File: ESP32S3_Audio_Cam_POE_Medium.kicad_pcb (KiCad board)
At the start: 2 copper layers, 97.8 x 70.5 mm, 241 parts, among them CN1 PJ-316C-6A, J1 Connector, USB-TYPE-C-16P, J10 Conn_01x02, J11 Conn_01x03, J12 Conn_01x02, J13 Conn_01x02, J14 Conn_01x03, J15 Conn_01x02, J16 Conn_01x02, J17 Conn_01x20_Pin, J18 Conn_01x20_Pin, J2 Conn_01x02, J3 Conn_01x02, J4 Conn_01x02, J5 Conn_01x02, J6 Conn_01x02, J7 Conn_01x03, J8 Conn_01x03, J9 Conn_01x02, Q1 AO3401A, Q2 AO3401A, Q3 AO3401A, Q4 AO3401A, Q5 AO3401A, Q6 AO3401A, Q7 AO3401A, U1 MT9221CT-06BR5, U10 ICS-43434, U11 ICS-43434, U3 USBLC6-2SC6, U4 ESP32-S3, U5 AXP2101, U6 DS18B20U(UMW), U7 W25Q128JVSIQ, U8 MAX98357AETE+T, U9 TM1637, Y1 40MHz, 15pF, Y2 32.768KHz

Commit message: DRAFT Medium
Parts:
- removed R12, R15: 100kΩ, PCM_JLCPCB:R_0402
- removed R14, R16: 10kΩ, PCM_JLCPCB:R_0402
- removed TP26: TestPoint, TestPoint:TestPoint_Pad_D1.0mm
- added J19: Conn_01x03, Connector_PinHeader_2.54mm:PinHeader_1x03_P2.54mm_Vertical, F.Cu at (124.7, 133.9)
- added TST-R1: 0Ω, PCM_JLCPCB:R_0603, F.Cu at (64.1, 138.2)
- TP10, TP12, TP13, TP6, TP8: moved to B.Cu
- moved C18 16.9 mm to (87.5, 146.8)
- moved D4 16.9 mm to (87.5, 144.9)
- moved TP25 16.9 mm to (89.8, 145.5)
- moved TST-R9 16.9 mm to (87.5, 148.1)
- moved TP6 16.1 mm to (106.2, 137.5)
- moved TP8 14.4 mm to (104.8, 139.1)
- moved TP19 13.8 mm to (111.0, 147.3)
- moved TP45 12.9 mm to (101.6, 150.1)
- moved TP5 12.2 mm to (100.6, 148.2)
- moved C1 11.2 mm to (84.8, 158.1)
- moved U1 11.2 mm to (90.6, 158.1)
- moved C2 11.2 mm to (95.0, 159.4)
- moved TP13 11.2 mm to (107.7, 150.1)
- moved TP17 9.49 mm to (112.6, 148.5)
- moved TST-R6 8.21 mm to (80.8, 135.6), turned to 0 degrees
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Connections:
- net /2GPIO41 renamed /RC.TILT
- net /VBus.Sense renamed /2GPIO14
- net Net-(U4-GPIO10) renamed /2GPIO10
- net Net-(U4-GPIO11) renamed /2GPIO11
- net Net-(U4-GPIO12) renamed /2GPIO12
- net Net-(U4-GPIO13) renamed /2GPIO13
- net Net-(U4-GPIO9) renamed /2GPIO9
- D1 pad 1: VBUS -> Vdrive
- J11 pad 1: /2GPIO40 -> /RC.ROT
- J14 pad 1: /2GPIO39 -> /RC.OTHR
- J7 pad 1: /2GPIO42 -> /RC.PAN
- JP1 pad 1: Vdrive -> Vdrive2
- R11 pad 2: /2USB_D- -> Net-(R11-Pad2)
- R13 pad 2: /2USB_D+ -> Net-(R13-Pad2)
- R32 pad 2: /2GPIO45 -> /RC.PWR
- R40 pad 1: Vdrive -> Vdrive2
- TP5 pad 1: /PMU.Vref -> Net-(U4-SPICS1)
- TST-R10 pad 2: Vdrive -> Vdrive2
- TST-R11 pad 2: Vdrive -> Vdrive2
- TST-R12 pad 2: Vdrive -> Vdrive2
- TST-R14 pad 2: Vdrive -> Vdrive2
- TST-R16 pad 1: Vdrive -> Vdrive2
- TST-R18 pad 1: Vdrive -> Vdrive2
- TST-R19 pad 2: Vdrive -> Vdrive2
- TST-R20 pad 2: +3V3 -> Vdrive2
- TST-R21 pad 2: +3V3 -> Vdrive2
- TST-R22 pad 2: +3V3 -> Vdrive2
- TST-R6 pad 1: VBUS -> Vdrive
- TST-R7 pad 2: Vdrive -> Vdrive2
- TST-R8 pad 2: Vdrive -> Vdrive2
- U1 pad 1: +3V3 -> Vdrive
- U1 pad 2: +3V3 -> Vdrive
- U3 pad 1: /2USB_D- -> Net-(R11-Pad2)
- U3 pad 3: /2USB_D+ -> Net-(R13-Pad2)
- U4 pad 23: /ISEN.VO -> /TEMP.DQ
- U4 pad 24: /TEMP.DQ -> /ISEN.VO
- U4 pad 28: /PMU.Vref -> Net-(U4-SPICS1)
- U4 pad 44: /2GPIO39 -> /RC.PWR
- U4 pad 45: /2GPIO40 -> /RC.PAN
- U4 pad 48: /2GPIO42 -> /RC.ROT
- U4 pad 51: /2GPIO45 -> /RC.OTHR
- U4 pad 52: /2GPIO46 -> /RC.OTHR2
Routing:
- net Vdrive2: track 0.00 -> 264.2 mm, vias 0 -> 11
- net Vdrive: track 27.3 -> 127.6 mm, vias 2 -> 0
- net /PMU.SCK: track 1.62 -> 75.1 mm, vias 1 -> 2
- net /PMU.SDA: track 1.18 -> 73.2 mm, vias 1 -> 2
- net /U0TXD: track 0.00 -> 59.9 mm, vias 0 -> 1
- net /U0RXD: track 0.00 -> 59.9 mm, vias 0 -> 1
- net COM: track 74.3 -> 119.6 mm, vias 59 -> 237
- net 2VDD_SPI: track 0.00 -> 29.7 mm
- net /MISC.OUT3: track 0.00 -> 29.3 mm
- net /TEMP.DQ: track 0.00 -> 29.2 mm, vias 0 -> 2
- net Net-(U4-VDD3P3_RTC): track 0.00 -> 29.1 mm
- net /MISC.OUT1: track 0.00 -> 26.7 mm
- net /MISC.OUT2: track 0.00 -> 26.6 mm
- net /2FLASH_QSPI_nCS: track 0.00 -> 25.4 mm
- net /RC.OTHR2: track 0.00 -> 23.0 mm
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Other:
- board size 97.8 x 70.5 mm -> 97.8 x 71.1 mm

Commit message: Draft Medium re-annotated.
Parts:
- renumbered C2 to C1, C19 to C10, C20 to C11, C9 to C12, C10 to C13, C59 to C14, C60 to C15, C54 to C16, C28 to C17, C30 to C18, C39 to C19, C23 to C2, C45 to C20, C55 to C21, C27 to C23, C33 to C24, C34 to C25, C35 to C26, C36 to C27, C41 to C28, C42 to C29, C1 to C3, C43 to C30, C47 to C31, C50 to C32, C51 to C33, C11 to C34, C12 to C35, C13 to C36, C14 to C37, C15 to C38, C61 to C39, C21 to C4, C62 to C40, C53 to C41, C56 to C42, C40 to C43, C26 to C44, C29 to C45, C31 to C46, C44 to C47, C52 to C48, C32 to C49, C24 to C5, C46 to C50, C48 to C51, C37 to C52, C38 to C53, C49 to C54, C17 to C55, C18 to C56, C16 to C57, C25 to C6, C57 to C7, C58 to C8, C8 to C9, D7 to D2, D9 to D3, D2 to D4, D8 to D6, D4 to D7, D3 to D8, D6 to D9, J5 to J10, J9 to J11, J7 to J12, J8 to J13, J11 to J14, J14 to J15, J19 to J16, J10 to J17, J6 to J18, J3 to J19, J17 to J2, J18 to J3, J16 to J4, J15 to J5, J4 to J6, J13 to J7, J12 to J8, J2 to J9, JP3 to JP2, JP4 to JP3, JP5 to JP4, JP6 to JP5, JP7 to JP6, JP2 to JP7, L4 to L1, L3 to L2, L5 to L3, L7 to L4, L6 to L5, L8 to L6, L9 to L7, PB2 to PB1, PB3 to PB2, PB4 to PB3, PB5 to PB4, PB1 to PB5, Q3 to Q2, Q6 to Q3, Q5 to Q4, Q2 to Q5, Q4 to Q6, R28 to R1, R6 to R10, R9 to R11, R42 to R12, R30 to R13, R39 to R14, R38 to R15, R17 to R16, R23 to R17, R33 to R18, R21 to R19, R8 to R2, R27 to R20, R36 to R21, R18 to R22, R24 to R23, R34 to R24, R31 to R25, R32 to R26, R7 to R27, R19 to R28, R25 to R29, R10 to R3, R35 to R30, R22 to R31, R29 to R32, R37 to R33, R26 to R34, R20 to R35, R11 to R4, R13 to R5, R40 to R6, R41 to R7, R43 to R8, R44 to R9, TP53 to TP1, TP11 to TP10, TP20 to TP11, TP21 to TP12, TP22 to TP13, TP23 to TP14, TP24 to TP15, TP18 to TP16, TP48 to TP17, TP50 to TP18, TP47 to TP19, TP55 to TP2, TP49 to TP20, TP27 to TP21, TP31 to TP22, TP35 to TP23, TP39 to TP24, TP46 to TP25, TP51 to TP26, TP28 to TP27, TP32 to TP28, TP36 to TP29, TP52 to TP3, TP40 to TP30, TP43 to TP31, TP29 to TP32, TP37 to TP34, TP41 to TP35, TP5 to TP36, TP10 to TP37, TP12 to TP38, TP13 to TP39, TP54 to TP4, TP14 to TP40, TP15 to TP41, TP16 to TP42, TP17 to TP43, TP19 to TP44, TP30 to TP45, TP34 to TP46, TP38 to TP47, TP42 to TP48, TP44 to TP49, TP4 to TP5, TP45 to TP50, TP25 to TP51, TST-R6 to TST-R1, TST-R24 to TST-R10, TST-R15 to TST-R11, TST-R13 to TST-R12, TST-R1 to TST-R13, TST-R7 to TST-R14, TST-R10 to TST-R15, TST-R14 to TST-R16, TST-R12 to TST-R18, TST-R9 to TST-R19, TST-R20 to TST-R2, TST-R8 to TST-R20, TST-R11 to TST-R21, TST-R16 to TST-R22, TST-R4 to TST-R3, TST-R18 to TST-R4, TST-R19 to TST-R5, TST-R21 to TST-R6, TST-R23 to TST-R7, TST-R5 to TST-R8, TST-R22 to TST-R9, U6 to U10, U3 to U2, U9 to U3, U8 to U4, U10 to U5, U11 to U6, U4 to U7, U5 to U8, U7 to U9

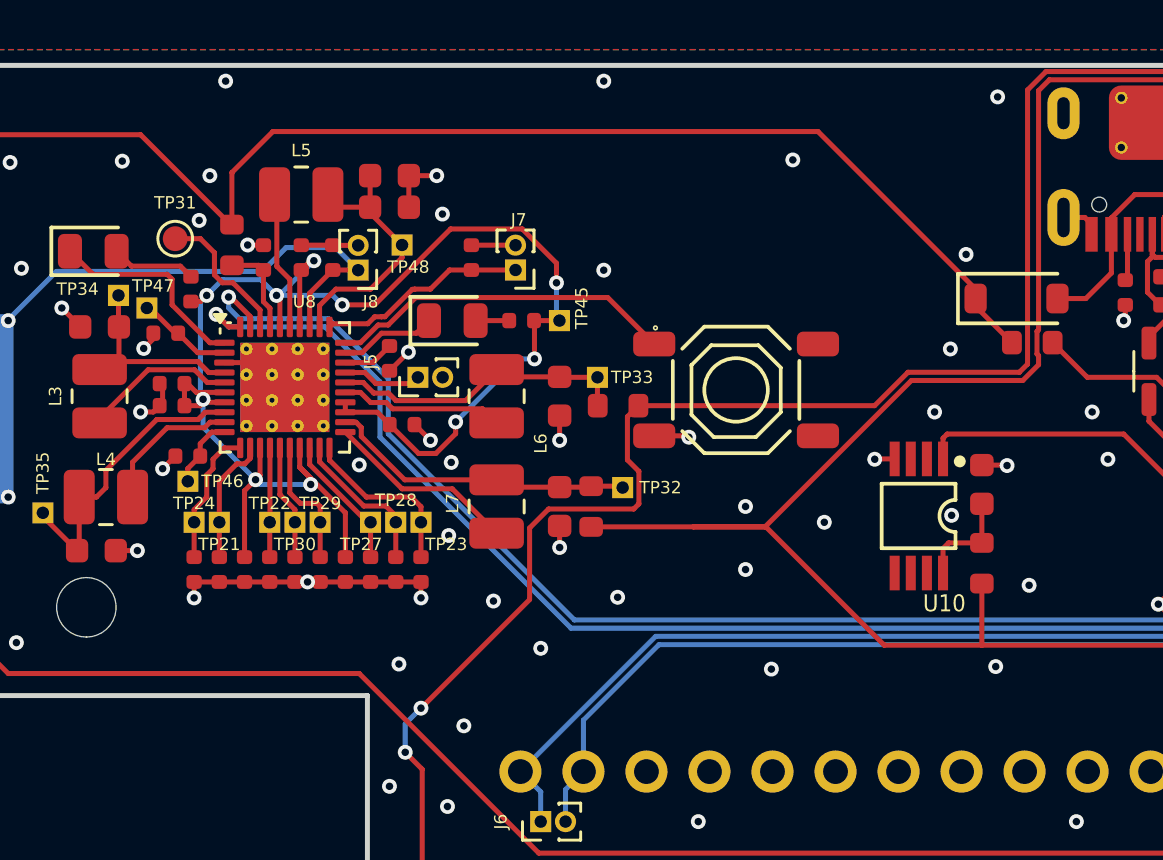
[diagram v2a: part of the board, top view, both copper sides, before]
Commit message: Changed Vdrive2 net from PMU.Vo1 to VDCDC5
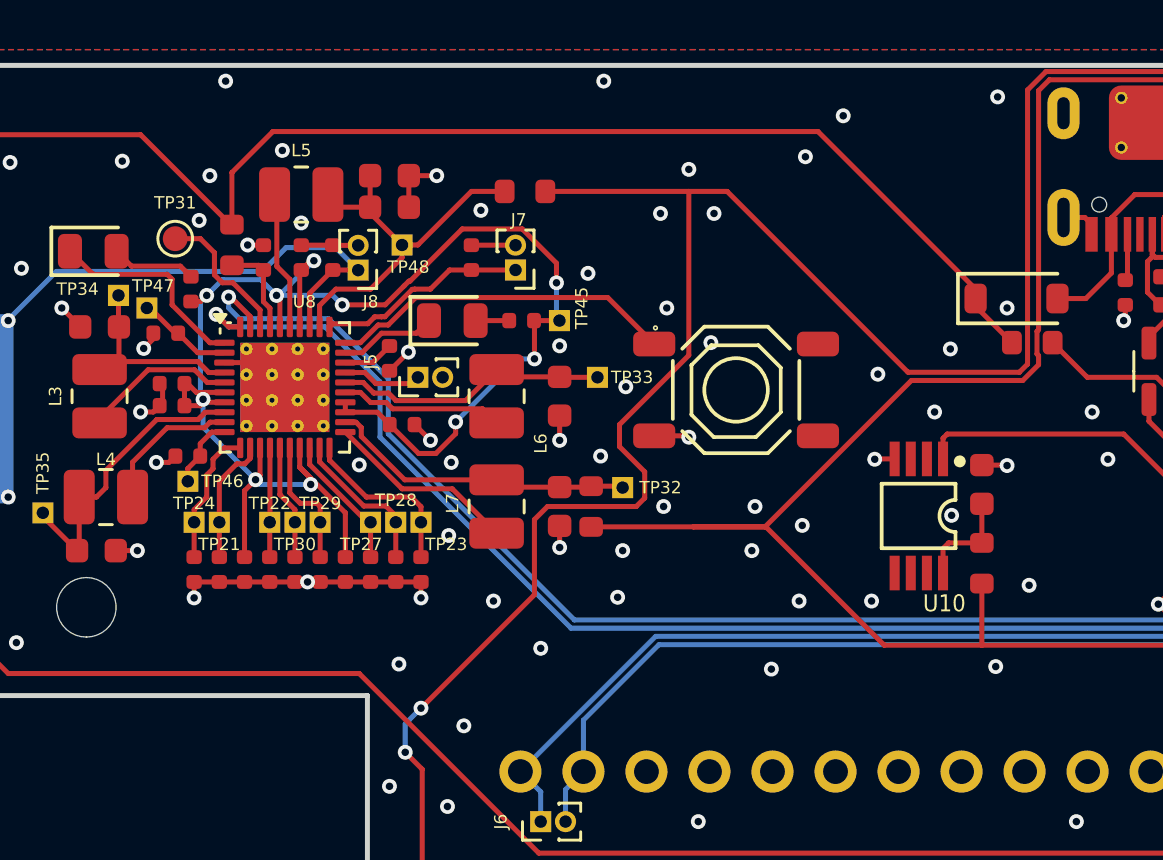
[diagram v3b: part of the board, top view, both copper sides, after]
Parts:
- moved TST-R13 9.42 mm to (60.3, 129.5)
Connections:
- TST-R13 pad 1: /PMU.Vo2 -> /VDCDC5
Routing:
- net Vdrive2: track 264.2 -> 280.5 mm
- net /VDCDC5: track 10.7 -> 15.8 mm
- net /PMU.Vo2: track 12.3 -> 11.1 mm
- net COM: track 119.6 -> 119.7 mm, vias 237 -> 253
